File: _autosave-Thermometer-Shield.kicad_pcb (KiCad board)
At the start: 2 copper layers, 31 parts, among them J1 CONN_01X04, J2 CONN_01X02, J3 CONN_01X02, J4 CONN_01X02, J5 CONN_01X02, SW1 SW_SPST, SW2 SW_SPST, SW3 SW_SPST, SW4 SW_SPST, U1 ULN2803A

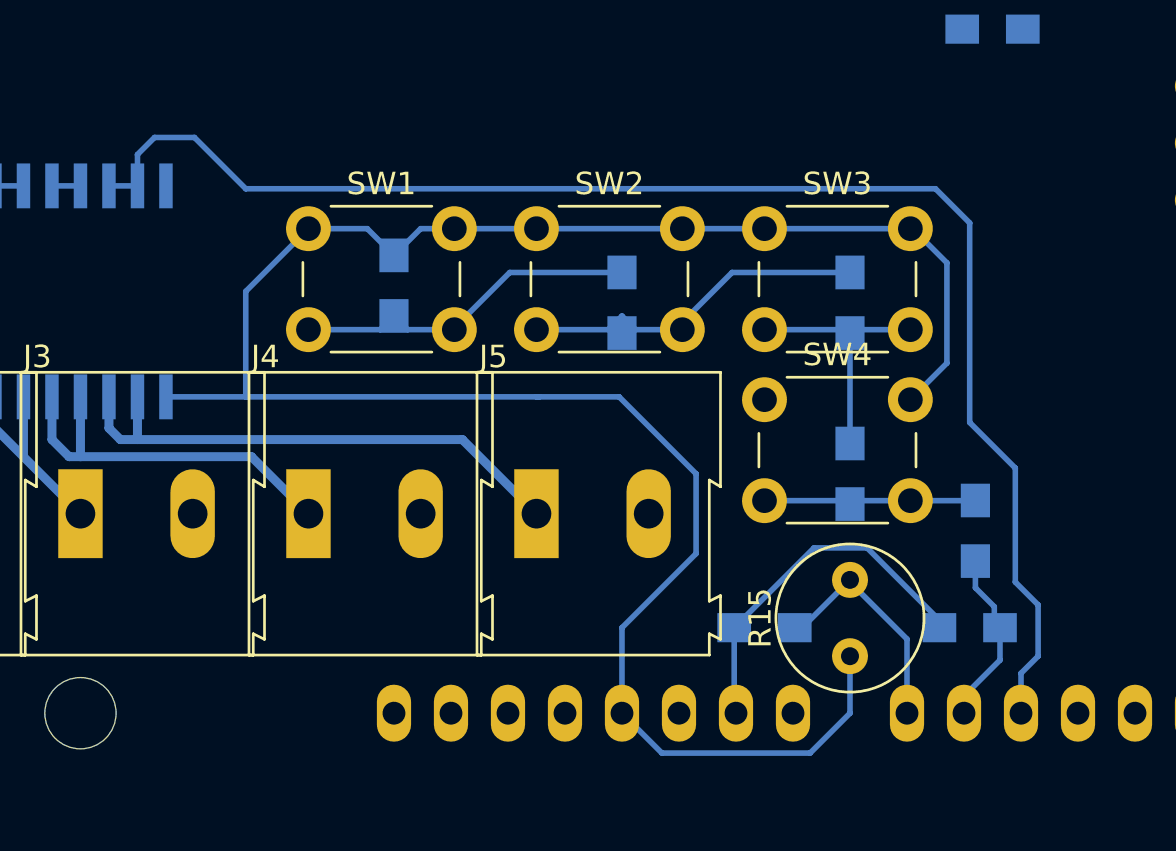
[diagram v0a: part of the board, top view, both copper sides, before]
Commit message: added documetation of parts, and some rework for more features
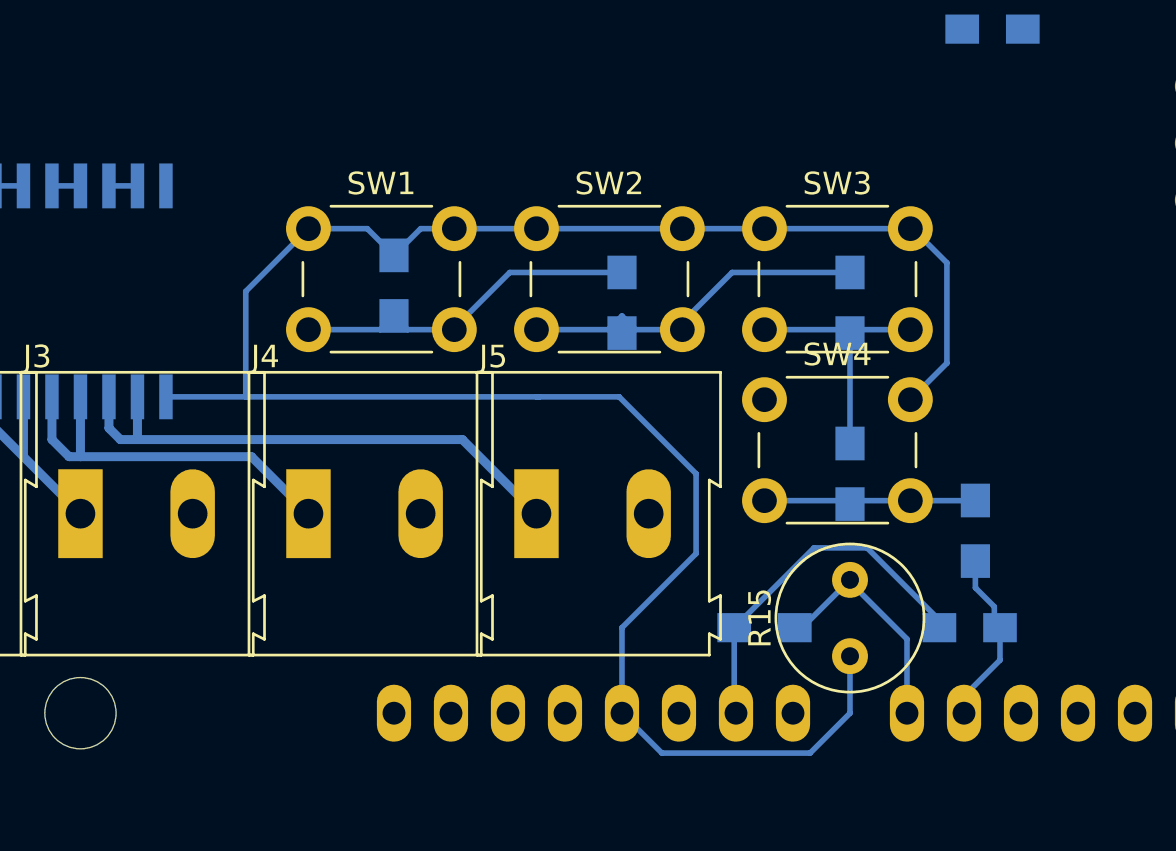
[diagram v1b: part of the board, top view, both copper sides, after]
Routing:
- net Trig-D: track 65.1 -> 1.27 mm
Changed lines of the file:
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@@
   (general
     (links 82)
-    (no_connects 42)
+    (no_connects 43)
     (area 64.494999 19.373 217.560501 115.523333)
     (thickness 1.6)
     (drawings 0)
-    (tracks 111)
+    (tracks 98)
     (zones 0)
     (modules 31)
@@
     (pad_to_mask_clearance 0)
     (aux_axis_origin 0 0)
-    (visible_elements FFFEBF7F)
+    (visible_elements FFFEFF7F)
     (pcbplotparams
       (layerselection 0x00030_80000001)
@@
   (segment (start 165.1 89.408) (end 179.578 89.408) (width 0.4) (layer B.Cu) (net 37))
   (segment (start 163.83 88.9) (end 164.338 89.408) (width 0.4) (layer B.Cu) (net 37))
-  (segment (start 167.64 75.946) (end 165.862 75.946) (width 0.25) (layer B.Cu) (net 38))
-  (segment (start 204.47 99.822) (end 205.232 99.06) (width 0.25) (layer B.Cu) (net 38))
-  (segment (start 205.232 99.06) (end 205.232 96.774) (width 0.25) (layer B.Cu) (net 38))
-  (segment (start 205.232 96.774) (end 204.216 95.758) (width 0.25) (layer B.Cu) (net 38))
-  (segment (start 204.216 95.758) (end 204.216 90.678) (width 0.25) (layer B.Cu) (net 38))
-  (segment (start 204.216 90.678) (end 202.184 88.646) (width 0.25) (layer B.Cu) (net 38))
-  (segment (start 202.184 88.646) (end 202.184 79.756) (width 0.25) (layer B.Cu) (net 38))
-  (segment (start 202.184 79.756) (end 200.66 78.232) (width 0.25) (layer B.Cu) (net 38))
-  (segment (start 200.66 78.232) (end 169.926 78.232) (width 0.25) (layer B.Cu) (net 38))
-  (segment (start 169.926 78.232) (end 167.64 75.946) (width 0.25) (layer B.Cu) (net 38))
-  (segment (start 204.47 101.6) (end 204.47 99.822) (width 0.25) (layer B.Cu) (net 38))
-  (segment (start 165.1 76.708) (end 165.1 78.104) (width 0.25) (layer B.Cu) (net 38))
-  (segment (start 165.862 75.946) (end 165.1 76.708) (width 0.25) (layer B.Cu) (net 38))
   (segment (start 163.83 78.104) (end 165.1 78.104) (width 0.25) (layer B.Cu) (net 38))
   (segment (start 161.29 78.104) (end 162.56 78.104) (width 0.25) (layer B.Cu) (net 39))
